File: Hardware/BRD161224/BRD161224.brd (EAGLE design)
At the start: 27.9 x 26.7 mm, 20 parts, among them Q1 DMP2035, Q2 FDV301, Q3 FDV301, Q4 DMP2035, Q5 DMP2035, Q6 DMP2035, Q7 FDV301

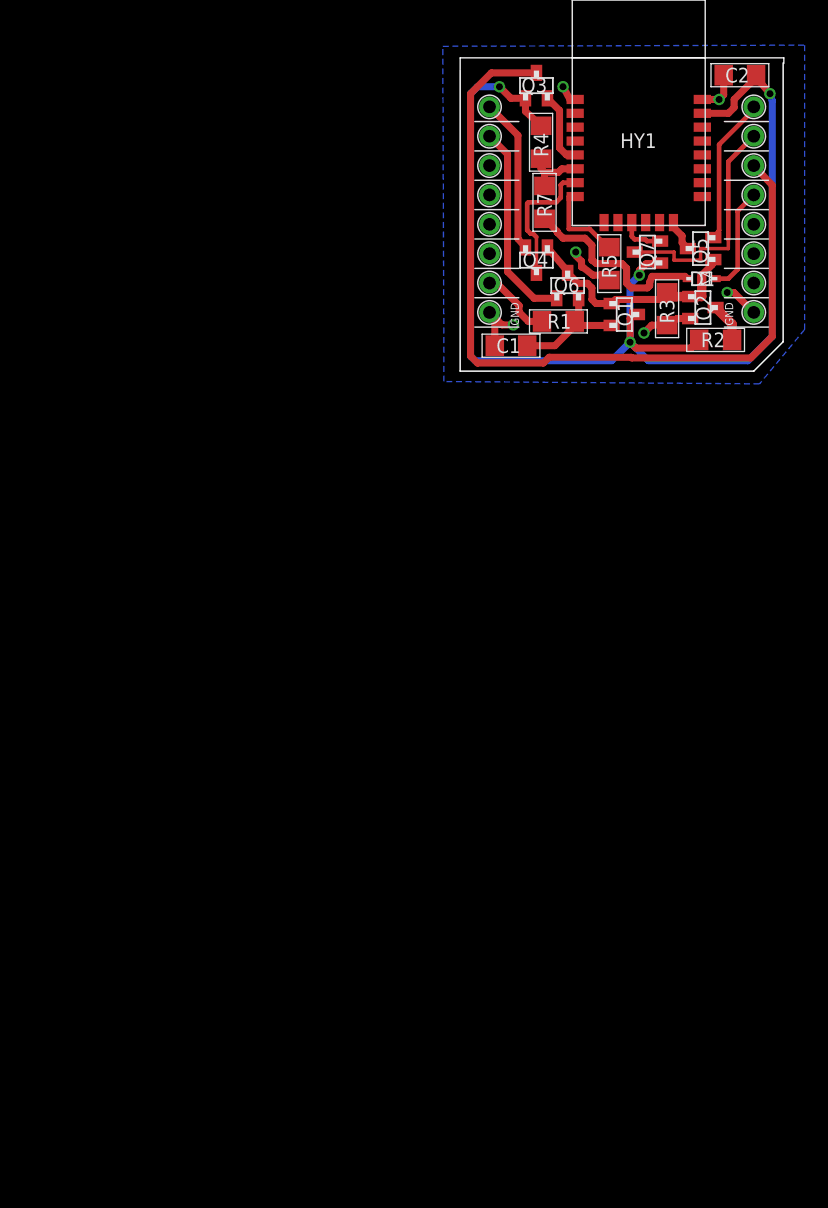
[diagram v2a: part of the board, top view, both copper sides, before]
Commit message: Schematic: replacing D1, R7 and R4 by Q8.
Signed-off-by: Christoph Tack <prog.send@gmail.com>
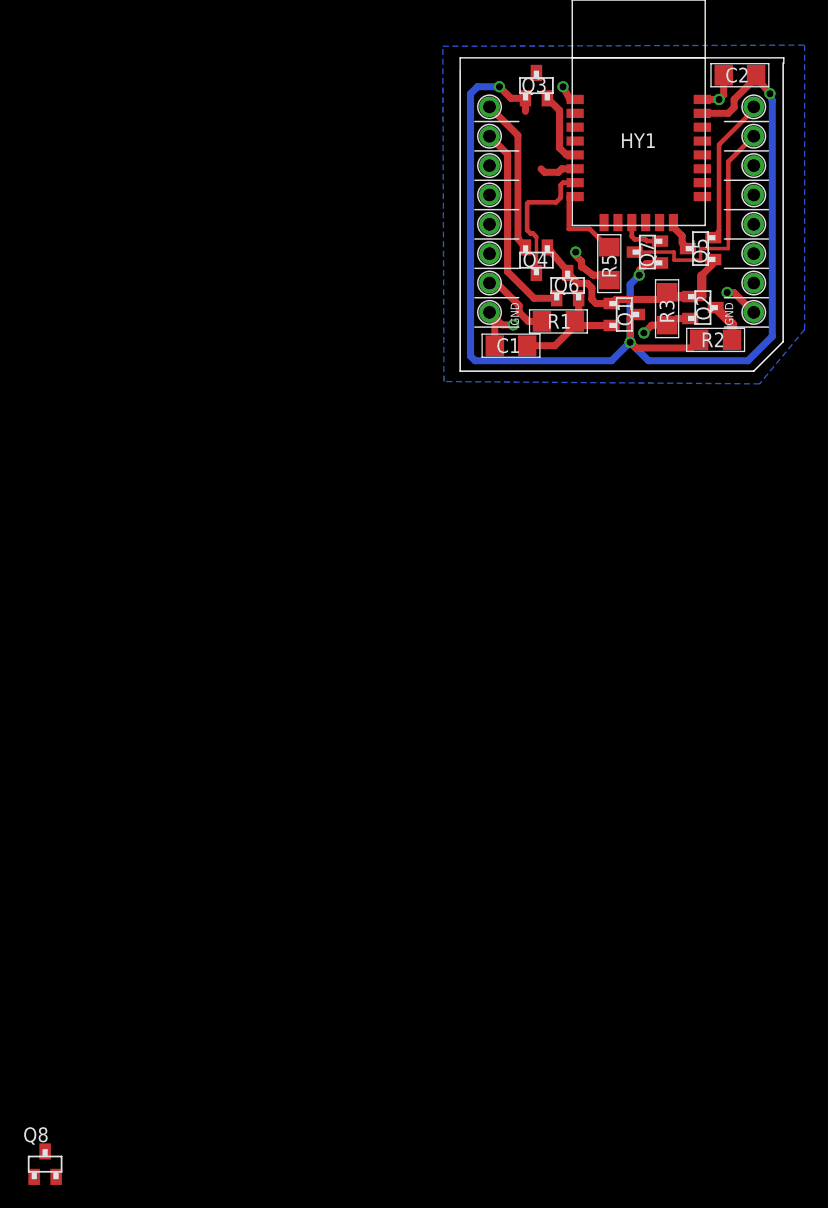
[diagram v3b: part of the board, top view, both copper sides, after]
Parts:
- removed D1: BAT46W, lieBtrau:SC_SOD323_ST
- removed R4: 100K, lieBtrau:RE_1206
- removed R7: 0E, lieBtrau:RE_1206
- added Q8: DMP2035, lieBtrau:SC_SOT23
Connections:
- removed net N$9 (its old number): D1.C, MC1.P$13
- net N$16: now also Q8.3; no longer R4.1, R7.2
- net N$2: no longer R4.2
- net N$4: now also Q8.1
- net N$8: now also MC1.P$13, Q8.2; no longer D1.A, R7.1
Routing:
- net N$9: track 71.9 -> 0.00 mm
- net N$8: track 17.2 -> 0.00 mm
- net N$9 (its old number): track 9.20 -> 0.00 mm
- net N$16: track 5.25 -> 3.20 mm
- net N$2: track 107.0 -> 105.1 mm
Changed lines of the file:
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@@
 <?xml version="1.0" encoding="utf-8"?>
 <!DOCTYPE eagle SYSTEM "eagle.dtd">
-<eagle version="8.1.1">
+<eagle version="8.2.2">
 <drawing>
 <settings>
@@
 <attribute name="ORDERCODE" value="FDV301NCT-ND" x="21" y="5.5" size="1.778" layer="27" rot="R270" display="off"/>
 </element>
-<element name="D1" library="lieBtrau" package="SC_SOD323_ST" value="BAT46W" x="20.9" y="8" smashed="yes" rot="R180">
-<attribute name="COST" value="0.34" x="20.9" y="8" size="1.778" layer="27" rot="R180" display="off"/>
-<attribute name="NAME" x="19.85" y="7.35" size="1.27" layer="25"/>
-<attribute name="ORDERCODE" value="568-6017-1-ND" x="20.9" y="8" size="1.778" layer="27" rot="R180" display="off"/>
-</element>
-<element name="R4" library="lieBtrau" package="RE_1206" value="100K" x="7" y="19.8" smashed="yes" rot="R90">
-<attribute name="COST" value="0.09" x="7" y="19.8" size="1.778" layer="27" rot="R90" display="off"/>
-<attribute name="NAME" x="7.63" y="18.53" size="1.27" layer="25" rot="R90"/>
-<attribute name="ORDERCODE" value="311-100KFRCT-ND" x="7" y="19.8" size="1.778" layer="27" rot="R90" display="off"/>
-</element>
 <element name="Q3" library="lieBtrau" package="SC_SOT23" value="FDV301" x="6.6" y="24.7" smashed="yes">
 <attribute name="COST" value="0.21" x="6.6" y="24.7" size="1.778" layer="27" display="off"/>
@@
 <attribute name="ORDERCODE" value="311-100KFRCT-ND" x="17.9" y="5.4" size="1.778" layer="27" rot="R90" display="off"/>
 </element>
-<element name="R7" library="lieBtrau" package="RE_1206" value="0E" x="7.3" y="14.6" smashed="yes" rot="R90">
-<attribute name="COST" value="0.09" x="7.3" y="14.6" size="1.778" layer="27" rot="R90" display="off"/>
-<attribute name="NAME" x="7.93" y="13.33" size="1.27" layer="25" rot="R90"/>
-<attribute name="ORDERCODE" value="311-0.0ERCT-ND" x="7.3" y="14.6" size="1.778" layer="27" rot="R90" display="off"/>
-</element>
 <element name="Q7" library="lieBtrau" package="SC_SOT23" value="FDV301" x="16.2" y="10.3" smashed="yes" rot="R90">
 <attribute name="COST" value="0.21" x="16.2" y="10.3" size="1.778" layer="27" rot="R90" display="off"/>
@@
 </element>
 <element name="DRILEGEND" library="drilegend" package="DRILEGEND" value="" x="34.183996875" y="23.674"/>
+<element name="Q8" library="lieBtrau" package="SC_SOT23" value="DMP2035" x="-35.9" y="-68.6">
+<attribute name="COST" value="0.38" x="-35.9" y="-68.6" size="1.778" layer="27" display="off"/>
+<attribute name="ORDERCODE" value="DMP2035U-7DICT-ND" x="-35.9" y="-68.6" size="1.778" layer="27" display="off"/>
+</element>
 </elements>
 <signals>
@@
 <contactref element="Q1" pad="3"/>
 <contactref element="R2" pad="2"/>
-<contactref element="R4" pad="2"/>
 <contactref element="Q3" pad="1"/>
-<wire x1="7" y1="21.222" x2="5.65" y2="22.472" width="0.6096" layer="1"/>
 <wire x1="5.65" y1="22.472" x2="5.65" y2="23.6" width="0.6096" layer="1"/>
 <wire x1="5.65" y1="23.6" x2="4.4" y2="23.6" width="0.6096" layer="1"/>
@@
 <wire x1="8.6" y1="22.55" x2="7.55" y2="23.6" width="0.6096" layer="1"/>
 </signal>
-<signal name="N$10">
-<contactref element="MC1" pad="P$14"/>
-<contactref element="Q3" pad="3"/>
-<wire x1="25.4" y1="17.78" x2="27" y2="16.08" width="0.6096" layer="1"/>
-<wire x1="27" y1="16.08" x2="27" y2="3" width="0.6096" layer="1"/>
-<wire x1="0.9" y1="1.3" x2="0.9" y2="24" width="0.6096" layer="1"/>
-<wire x1="6.6" y1="25.8" x2="2.7" y2="25.8" width="0.6096" layer="1"/>
-<wire x1="2.7" y1="25.8" x2="0.9" y2="24" width="0.6096" layer="1"/>
-<wire x1="0.9" y1="1.3" x2="1.5" y2="0.7" width="0.6096" layer="1"/>
-<wire x1="7.2" y1="0.7" x2="7.7" y2="1.2" width="0.6096" layer="1"/>
-<wire x1="7.7" y1="1.2" x2="14.7843375" y2="1.2" width="0.6096" layer="1"/>
-<wire x1="14.7843375" y1="1.2" x2="14.8439375" y2="1.1404" width="0.6096" layer="1"/>
-<wire x1="14.8439375" y1="1.1404" x2="25.1404" y2="1.1404" width="0.6096" layer="1"/>
-<wire x1="25.1404" y1="1.1404" x2="27" y2="3" width="0.6096" layer="1"/>
-<wire x1="1.5" y1="0.7" x2="7.2" y2="0.7" width="0.6096" layer="1"/>
-</signal>
 <signal name="N$11">
 <contactref element="HY1" pad="12"/>
@@
 <wire x1="15.1" y1="11.4" x2="14.85" y2="11.65" width="0.4064" layer="1"/>
 <wire x1="14.85" y1="11.65" x2="14.85" y2="12.85" width="0.4064" layer="1"/>
-</signal>
-<signal name="N$9">
-<contactref element="MC1" pad="P$13"/>
-<contactref element="D1" pad="C"/>
-<wire x1="22.15" y1="8" x2="23.2" y2="8" width="0.4064" layer="1"/>
-<wire x1="23.2" y1="8" x2="24" y2="8.8" width="0.4064" layer="1"/>
-<wire x1="24" y1="8.8" x2="24" y2="13.84" width="0.4064" layer="1"/>
-<wire x1="24" y1="13.84" x2="25.4" y2="15.24" width="0.4064" layer="1"/>
 </signal>
 <signal name="N$12">
@@
 <wire x1="11" y1="7.6" x2="11.4" y2="7.2" width="0.6096" layer="1"/>
 <wire x1="11.4" y1="7.2" x2="11.4" y2="6.2" width="0.6096" layer="1"/>
-</signal>
-<signal name="N$8">
-<contactref element="D1" pad="A"/>
-<contactref element="R7" pad="1"/>
-<wire x1="10.8" y1="11.5" x2="8.9" y2="11.5" width="0.6096" layer="1"/>
-<wire x1="8.9" y1="11.5" x2="8.4" y2="12" width="0.6096" layer="1"/>
-<wire x1="8.4" y1="12" x2="8.4" y2="12.078" width="0.6096" layer="1"/>
-<wire x1="8.4" y1="12.078" x2="7.3" y2="13.178" width="0.6096" layer="1"/>
-<wire x1="10.8" y1="11.5" x2="11.4" y2="10.9" width="0.6096" layer="1"/>
-<wire x1="11.4" y1="10.9" x2="11.4" y2="9.6" width="0.6096" layer="1"/>
-<wire x1="11.4" y1="9.6" x2="11.8" y2="9.3" width="0.6096" layer="1"/>
-<wire x1="11.8" y1="9.3" x2="14" y2="9.3" width="0.6096" layer="1"/>
-<wire x1="14" y1="9.3" x2="14.4" y2="8.9" width="0.6096" layer="1"/>
-<wire x1="14.4" y1="8.9" x2="14.4" y2="7.6" width="0.6096" layer="1"/>
-<wire x1="14.4" y1="7.6" x2="14.8" y2="7.2" width="0.6096" layer="1"/>
-<wire x1="14.8" y1="7.2" x2="16.2" y2="7.2" width="0.6096" layer="1"/>
-<wire x1="16.2" y1="7.2" x2="16.4" y2="7.4" width="0.6096" layer="1"/>
-<wire x1="16.4" y1="7.4" x2="16.4" y2="7.7" width="0.6096" layer="1"/>
-<wire x1="16.4" y1="7.7" x2="16.6" y2="8.2" width="0.6096" layer="1"/>
-<wire x1="16.6" y1="8.2" x2="19.45" y2="8.2" width="0.6096" layer="1"/>
-<wire x1="19.45" y1="8.2" x2="19.65" y2="8" width="0.6096" layer="1"/>
+<contactref element="Q8" pad="1"/>
+<wire x1="11.75" y1="5.85" x2="-36.85" y2="-69.7" width="0" layer="19" extent="1-1"/>
 </signal>
 <signal name="N$16">
-<contactref element="R4" pad="1"/>
-<contactref element="R7" pad="2"/>
 <contactref element="HY1" pad="6"/>
 <wire x1="9.95" y1="17.5" x2="8.8" y2="17.5" width="0.6096" layer="1"/>
 <wire x1="8.8" y1="17.5" x2="8.5" y2="17.2" width="0.6096" layer="1"/>
 <wire x1="8.5" y1="17.2" x2="7.3" y2="17.2" width="0.6096" layer="1"/>
-<wire x1="7.3" y1="17.2" x2="7.3" y2="16.022" width="0.6096" layer="1"/>
-<wire x1="7" y1="18.378" x2="7" y2="17.5" width="0.6096" layer="1"/>
 <wire x1="7" y1="17.5" x2="7.3" y2="17.2" width="0.6096" layer="1"/>
+<contactref element="Q8" pad="3"/>
+<wire x1="7.3" y1="17.2" x2="-35.9" y2="-67.5" width="0" layer="19" extent="1-1"/>
 </signal>
 <signal name="N$18">
@@
 <wire x1="18.5" y1="10.3" x2="15.1" y2="10.3" width="0.3048" layer="1"/>
 </signal>
+<signal name="N$8">
+<contactref element="MC1" pad="P$13"/>
+<contactref element="Q8" pad="2"/>
+<wire x1="25.4" y1="15.24" x2="-34.95" y2="-69.7" width="0" layer="19" extent="1-1"/>
+</signal>
+<signal name="N$9">
+<contactref element="Q3" pad="3"/>
+<contactref element="MC1" pad="P$14"/>
+<wire x1="6.6" y1="25.8" x2="25.4" y2="17.78" width="0" layer="19" extent="1-1"/>
+</signal>
 </signals>
